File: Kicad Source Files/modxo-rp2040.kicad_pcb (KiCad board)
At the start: 2 copper layers, 42.7 x 27.6 mm, 8 parts, among them J1 XBOX_LPC, U1 rp2040-zero

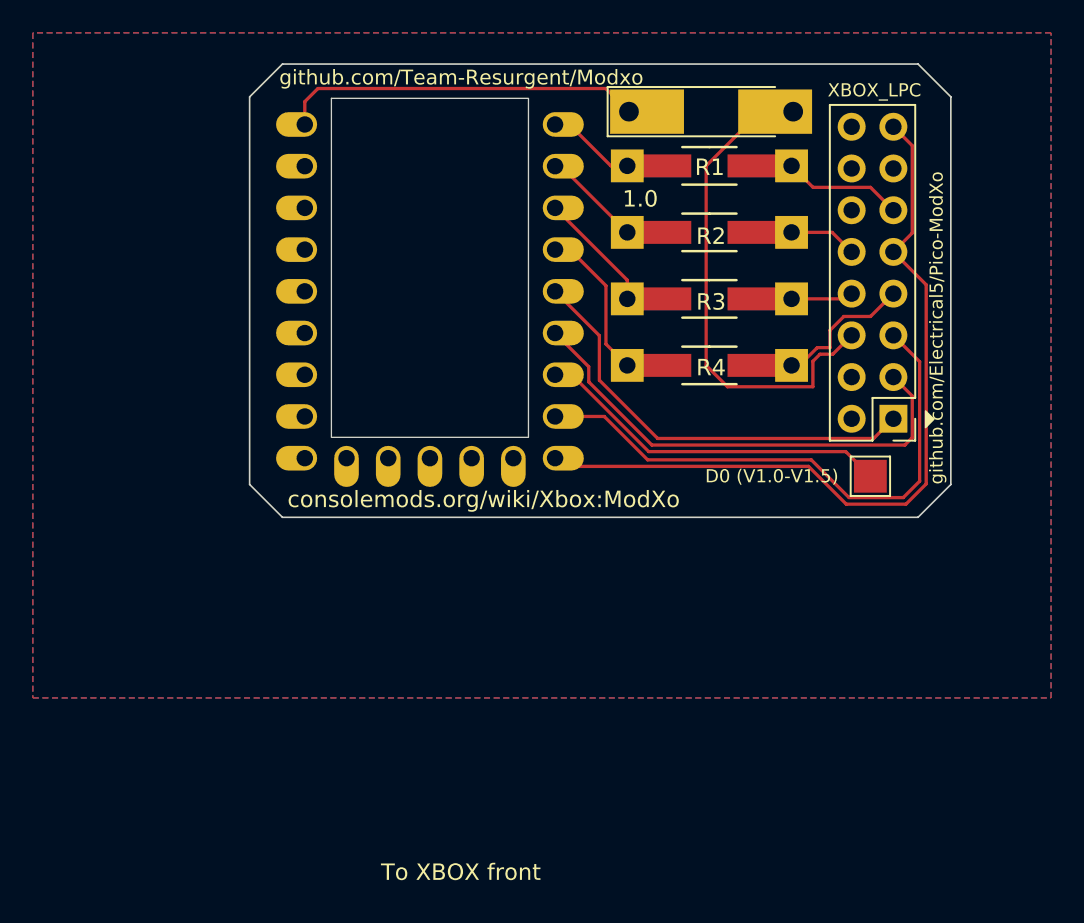
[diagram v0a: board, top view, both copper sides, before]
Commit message: Added logos
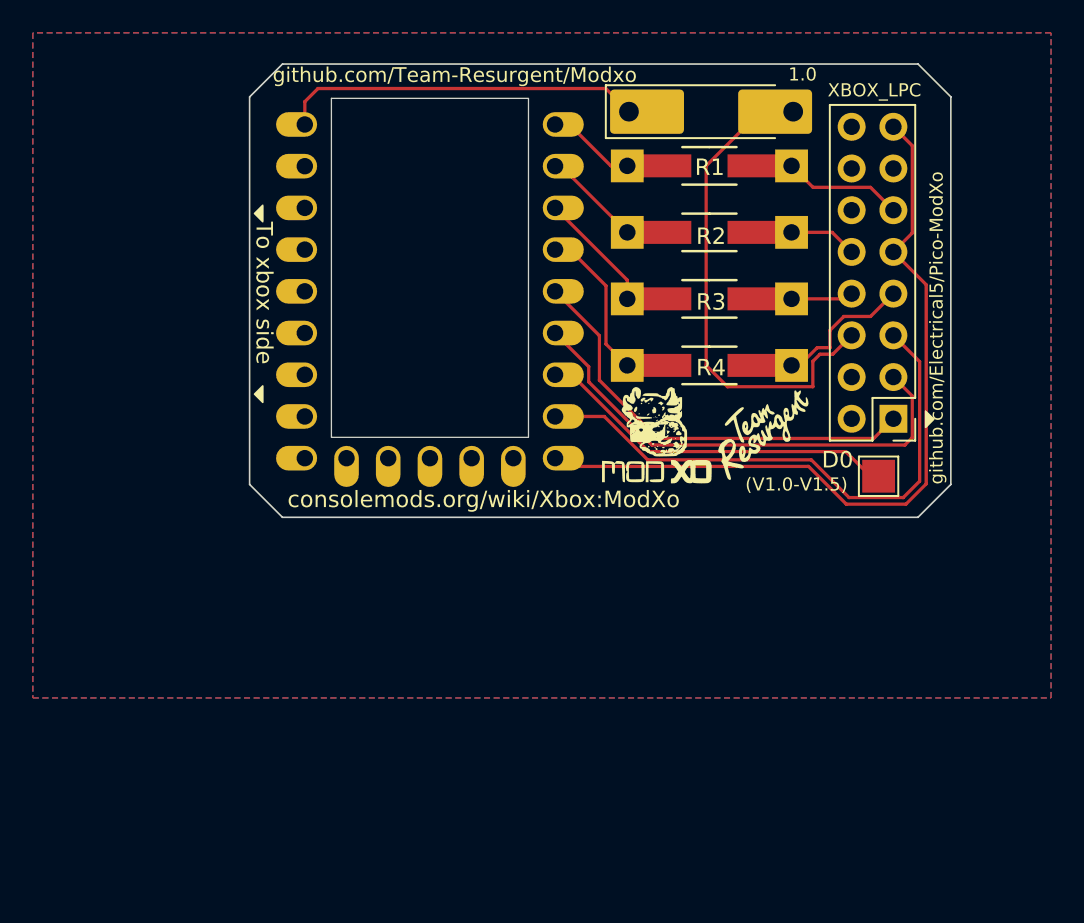
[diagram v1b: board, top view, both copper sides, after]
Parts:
- added G***: LOGO, xbox_lpc:team-resurgent, F.Cu at (168.0, 65.0)
- added G***: LOGO, xbox_lpc:modxo-logo, F.Cu at (161.5, 65.0)
- D0: value D0 (V1.0-V1.5) -> (V1.0-V1.5)
- moved D0 0.50 mm to (175.0, 67.5)
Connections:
- J1 pad 13: LSCL -> unconnected-(J1-SCL-Pad13)
- J1 pad 14: LSDA -> unconnected-(J1-SDA-Pad14)
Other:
- board text added: "To xbox side"
- board text removed: "To XBOX front"
